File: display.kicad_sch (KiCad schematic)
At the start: 2 parts, among them U11 AW9364DNR

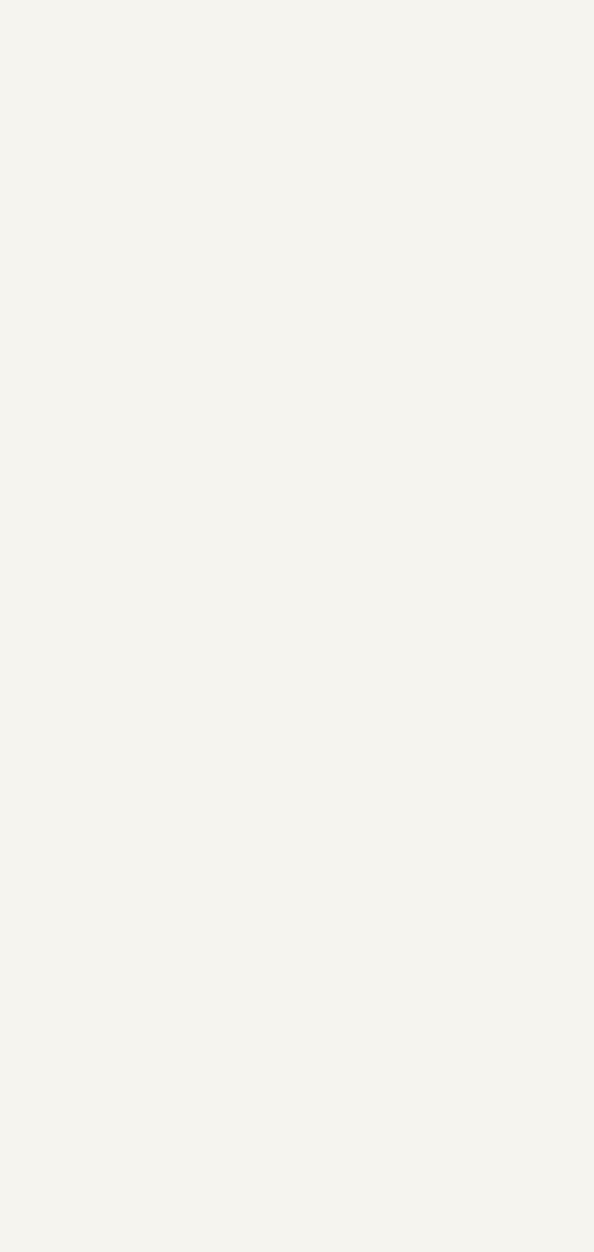
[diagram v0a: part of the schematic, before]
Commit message: Add FPC library
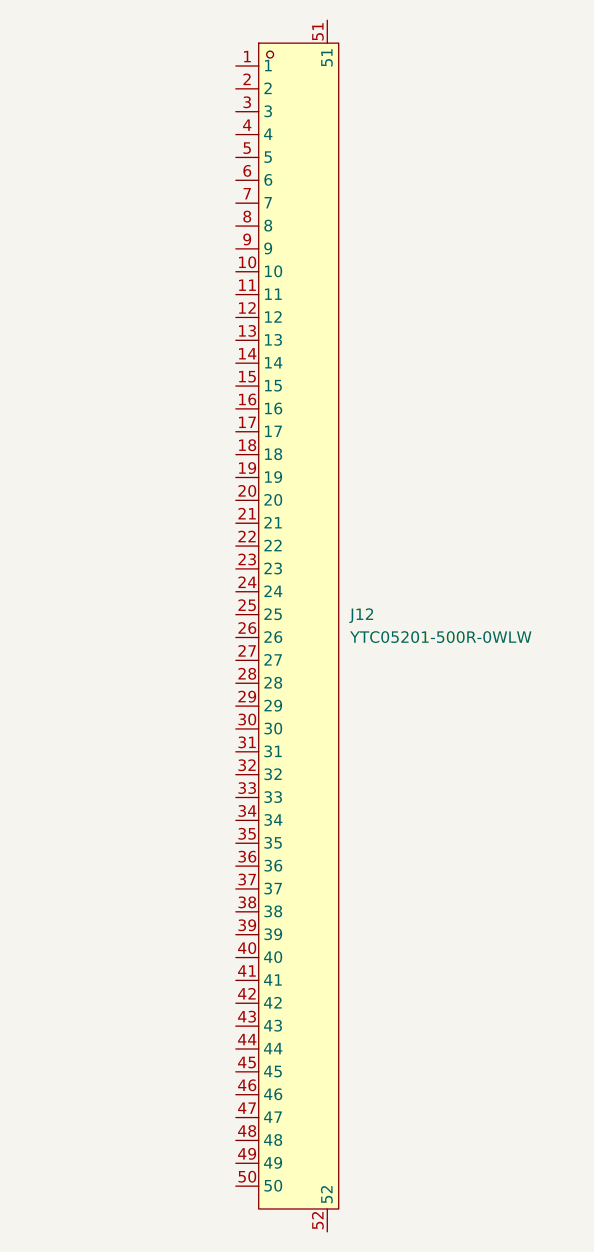
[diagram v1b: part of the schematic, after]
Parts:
- added J12: YTC05201-500R-0WLW, custom:FPC-SMD_50P-P0.50_YTC05201-500R-0WLW, symbol custom:YTC05201-500R-0WLW
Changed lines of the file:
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@@
+	)
+	(symbol
+		(lib_id "custom:YTC05201-500R-0WLW")
+		(at 147.32 101.6 0)
+		(unit 1)
+		(body_style 1)
+		(exclude_from_sim no)
+		(in_bom yes)
+		(on_board yes)
+		(in_pos_files yes)
+		(dnp no)
+		(fields_autoplaced yes)
+		(property "Reference" "J12"
+			(at 154.94 100.3299 0)
+			(show_name no)
+			(do_not_autoplace no)
+			(effects
+				(font
+					(size 1.27 1.27)
+				)
+				(justify left)
+			)
+		)
+		(property "Value" "YTC05201-500R-0WLW"
+			(at 154.94 102.8699 0)
+			(show_name no)
+			(do_not_autoplace no)
+			(effects
+				(font
+					(size 1.27 1.27)
+				)
+				(justify left)
+			)
+		)
+		(property "Footprint" "custom:FPC-SMD_50P-P0.50_YTC05201-500R-0WLW"
+			(at 147.32 176.53 0)
+			(hide yes)
+			(show_name no)
+			(do_not_autoplace no)
+			(effects
+				(font
+					(size 1.27 1.27)
+				)
+			)
+		)
+		(property "Datasheet" "https://www.lcsc.com/datasheet/C19673900.pdf"
+			(at 147.32 179.07 0)
+			(hide yes)
+			(show_name no)
+			(do_not_autoplace no)
+			(effects
+				(font
+					(size 1.27 1.27)
+				)
+			)
+		)
+		(property "Description" ""
+			(at 147.32 101.6 0)
+			(hide yes)
+			(show_name no)
+			(do_not_autoplace no)
+			(effects
+				(font
+					(size 1.27 1.27)
+				)
+			)
+		)
+		(property "Manufacturer" "YIYUAN(怡远)"
+			(at 147.32 181.61 0)
+			(hide yes)
+			(show_name no)
+			(do_not_autoplace no)
+			(effects
+				(font
+					(size 1.27 1.27)
+				)
+			)
+		)
+		(property "MPN" "YTC05201-500R-0WLW"
+			(at 147.32 184.15 0)
+			(hide yes)
+			(show_name no)
+			(do_not_autoplace no)
+			(effects
+				(font
+					(size 1.27 1.27)
+				)
+			)
+		)
+		(property "LCSC Part" "C19673900"
+			(at 147.32 186.69 0)
+			(hide yes)
+			(show_name no)
+			(do_not_autoplace no)
+			(effects
+				(font
+					(size 1.27 1.27)
+				)
+			)
+		)
+		(property "LCSC" "C19673900"
+			(at 147.32 191.77 0)
+			(hide yes)
+			(show_name no)
+			(do_not_autoplace no)
+			(effects
+				(font
+					(size 1.27 1.27)
+				)
+			)
+		)
+		(pin "42"
+		)
+		(pin "33"
+		)
+		(pin "43"
+		)
+		(pin "37"
+		)
+		(pin "44"
+		)
+		(pin "52"
+		)
+		(pin "39"
+		)
+		(pin "31"
+		)
+		(pin "32"
+		)
+		(pin "41"
+		)
+		(pin "45"
+		)
+		(pin "38"
+		)
+		(pin "46"
+		)
+		(pin "34"
+		)
+		(pin "36"
+		)
+		(pin "47"
+		)
+		(pin "48"
+		)
+		(pin "51"
+		)
+		(pin "40"
+		)
+		(pin "49"
+		)
+		(pin "50"
+		)
+		(pin "35"
+		)
+		(pin "3"
+		)
+		(pin "14"
+		)
+		(pin "16"
+		)
+		(pin "2"
+		)
+		(pin "10"
+		)
+		(pin "12"
+		)
+		(pin "1"
+		)
+		(pin "11"
+		)
+		(pin "25"
+		)
+		(pin "6"
+		)
+		(pin "9"
+		)
+		(pin "5"
+		)
+		(pin "13"
+		)
+		(pin "7"
+		)
+		(pin "8"
+		)
+		(pin "4"
+		)
+		(pin "15"
+		)
+		(pin "17"
+		)
+		(pin "18"
+		)
+		(pin "19"
+		)
+		(pin "20"
+		)
+		(pin "21"
+		)
+		(pin "22"
+		)
+		(pin "23"
+		)
+		(pin "24"
+		)
+		(pin "26"
+		)
+		(pin "27"
+		)
+		(pin "28"
+		)
+		(pin "29"
+		)
+		(pin "30"
+		)
+		(instances
+			(project "pedal"
+				(path "/e2443317-b83f-4e66-ac79-3186c6d613f3/fcca89f2-f5d5-44e1-8b43-7ff4c1465bba"
+					(reference "J12")
+					(unit 1)
+				)
+			)
+		)
 	)
 	(symbol

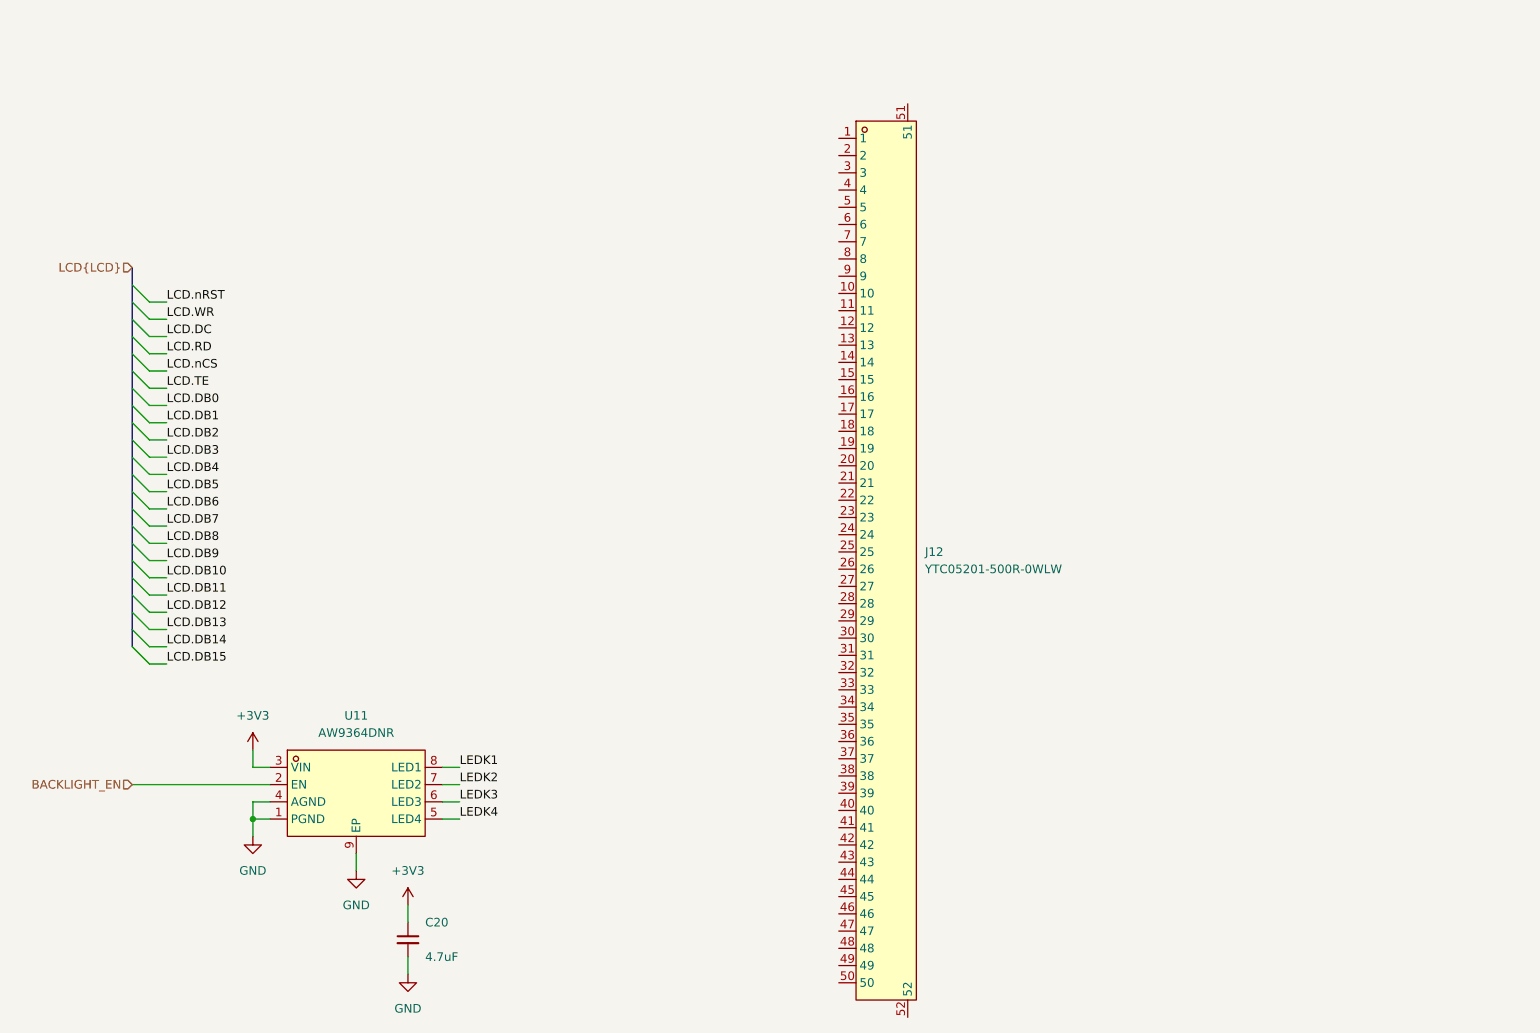
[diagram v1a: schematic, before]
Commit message: Add logic level shifters
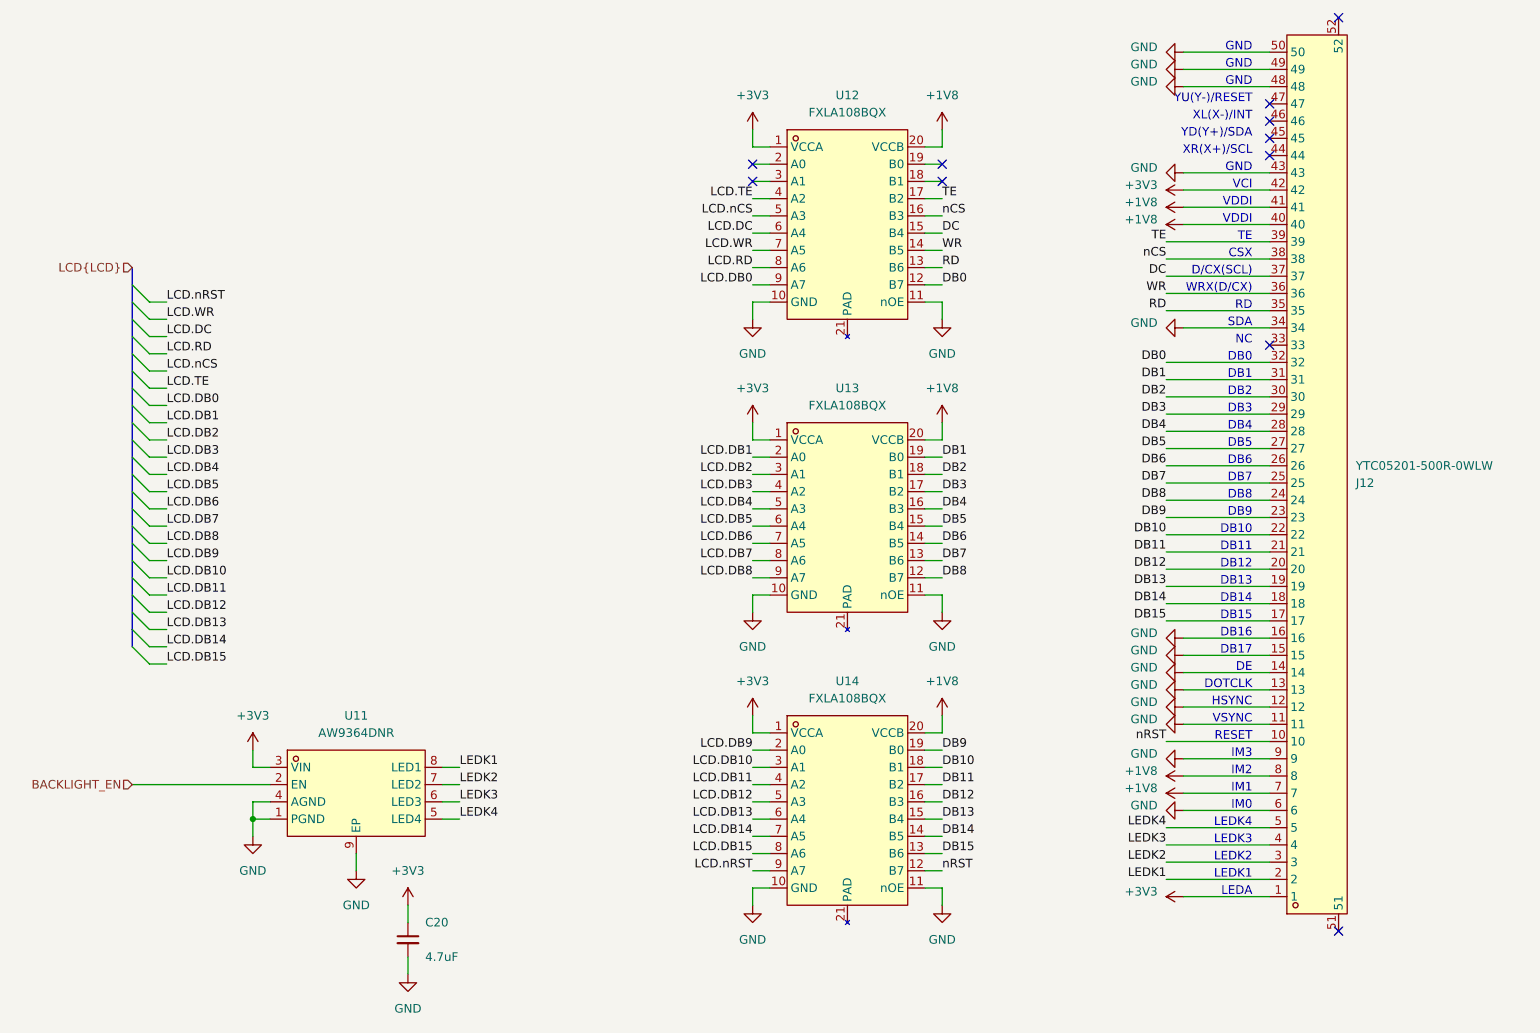
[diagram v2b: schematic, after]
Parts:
- added U12, U13, U14: FXLA108BQX, custom:DHVQFN-20_L4.5-W2.5-P0.50-BL-EP, symbol custom:FXLA108BQX
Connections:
- net +3V3: now also J12.1, J12.42, U12.1 (VCCA), U13.1 (VCCA), U14.1 (VCCA)
- net GND: now also J12.11, J12.12, J12.13, J12.14, J12.15, J12.16, J12.34, J12.43, J12.48, J12.49, J12.50, J12.6, J12.9, U12.10 (GND), U12.11 (nOE), U13.10 (GND), U13.11 (nOE), U14.10 (GND), U14.11 (nOE)
- net LCD.DB0: now also U12.9 (A7)
- net LCD.DB1: now also U13.2 (A0)
- net LCD.DB10: now also U14.3 (A1)
- net LCD.DB11: now also U14.4 (A2)
- net LCD.DB12: now also U14.5 (A3)
- net LCD.DB13: now also U14.6 (A4)
- net LCD.DB14: now also U14.7 (A5)
- net LCD.DB15: now also U14.8 (A6)
- net LCD.DB2: now also U13.3 (A1)
- net LCD.DB3: now also U13.4 (A2)
- net LCD.DB4: now also U13.5 (A3)
- net LCD.DB5: now also U13.6 (A4)
- net LCD.DB6: now also U13.7 (A5)
- net LCD.DB7: now also U13.8 (A6)
- net LCD.DB8: now also U13.9 (A7)
- net LCD.DB9: now also U14.2 (A0)
- net LCD.DC: now also U12.6 (A4)
- net LCD.RD: now also U12.8 (A6)
- net LCD.TE: now also U12.4 (A2)
- net LCD.WR: now also U12.7 (A5)
- net LCD.nCS: now also U12.5 (A3)
- net LCD.nRST: now also U14.9 (A7)
- net LEDK1: now also J12.2
- net LEDK2: now also J12.3
- net LEDK3: now also J12.4
- net LEDK4: now also J12.5
- net nRST: now reaches J12.10
- net nRST: now also U14.12 (B7)
- net DB15: now reaches J12.17
- net DB15: now also U14.13 (B6)
- net DB14: now reaches J12.18
- net DB14: now also U14.14 (B5)
- net DB13: now reaches J12.19
- net DB13: now also U14.15 (B4)
- net DB12: now reaches J12.20
- net DB12: now also U14.16 (B3)
- net DB11: now reaches J12.21
- net DB11: now also U14.17 (B2)
- net DB10: now reaches J12.22
- net DB10: now also U14.18 (B1)
- net DB9: now reaches J12.23
- net DB9: now also U14.19 (B0)
- net DB8: now reaches J12.24
- net DB8: now also U13.12 (B7)
- net DB7: now reaches J12.25
- net DB7: now also U13.13 (B6)
- net DB6: now reaches J12.26
- net DB6: now also U13.14 (B5)
- net DB5: now reaches J12.27
- net DB5: now also U13.15 (B4)
- net DB4: now reaches J12.28
- net DB4: now also U13.16 (B3)
- net DB3: now reaches J12.29
- net DB3: now also U13.17 (B2)
- net DB2: now reaches J12.30
- net DB2: now also U13.18 (B1)
- net DB1: now reaches J12.31
- net DB1: now also U13.19 (B0)
- net DB0: now reaches J12.32
- net DB0: now also U12.12 (B7)
- net RD: now reaches J12.35
- net RD: now also U12.13 (B6)
- net WR: now reaches J12.36
- net WR: now also U12.14 (B5)
- net DC: now reaches J12.37
- net DC: now also U12.15 (B4)
- net nCS: now reaches J12.38
- net nCS: now also U12.16 (B3)
- net TE: now reaches J12.39
- net TE: now also U12.17 (B2)
- net +1V8: now reaches J12.40
- net +1V8: now also J12.41, J12.7, J12.8, U12.20 (VCCB), U13.20 (VCCB), U14.20 (VCCB)
- no-connect marks 0 -> 11
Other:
- note added: "CSX"
- note added: "D/CX(SCL)"
- note added: "DB0"
- note added: "DB1"
- note added: "DB10"
- note added: "DB11"
- note added: "DB12"
- note added: "DB13"
- note added: "DB14"
- note added: "DB15"
- note added: "DB16"
- note added: "DB17"
- note added: "DB2"
- note added: "DB3"
- note added: "DB4"
- note added: "DB5"
- note added: "DB6"
- note added: "DB7"
- note added: "DB8"
- note added: "DB9"
- note added: "DE"
- note added: "DOTCLK"
- note added: "GND"
- note added: "HSYNC"
- note added: "IM0"
- note added: "IM1"
- note added: "IM2"
- note added: "IM3"
- note added: "LEDA"
- note added: "LEDK1"
- note added: "LEDK2"
- note added: "LEDK3"
- note added: "LEDK4"
- note added: "NC"
- note added: "RD"
- note added: "RESET"
- note added: "SDA"
- note added: "TE"
- note added: "VCI"
- note added: "VDDI"
- note added: "VSYNC"
- note added: "WRX(D/CX)"
- note added: "XL(X-)/INT"
- note added: "XR(X+)/SCL"
- note added: "YD(Y+)/SDA"
- note added: "YU(Y-)/RESET"
- moved on the sheet: J12
